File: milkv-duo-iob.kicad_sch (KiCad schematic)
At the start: 18 parts, among them J1 Conn_01x20_Socket, J10 Conn_01x02, J2 Conn_01x20_Socket, J3 Conn_01x05_Socket, J4 8P8C_Shielded, J5 Conn_01x20, J6 Conn_01x20, J7 Conn_01x12, J8 Conn_01x12, J9 Conn_01x04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

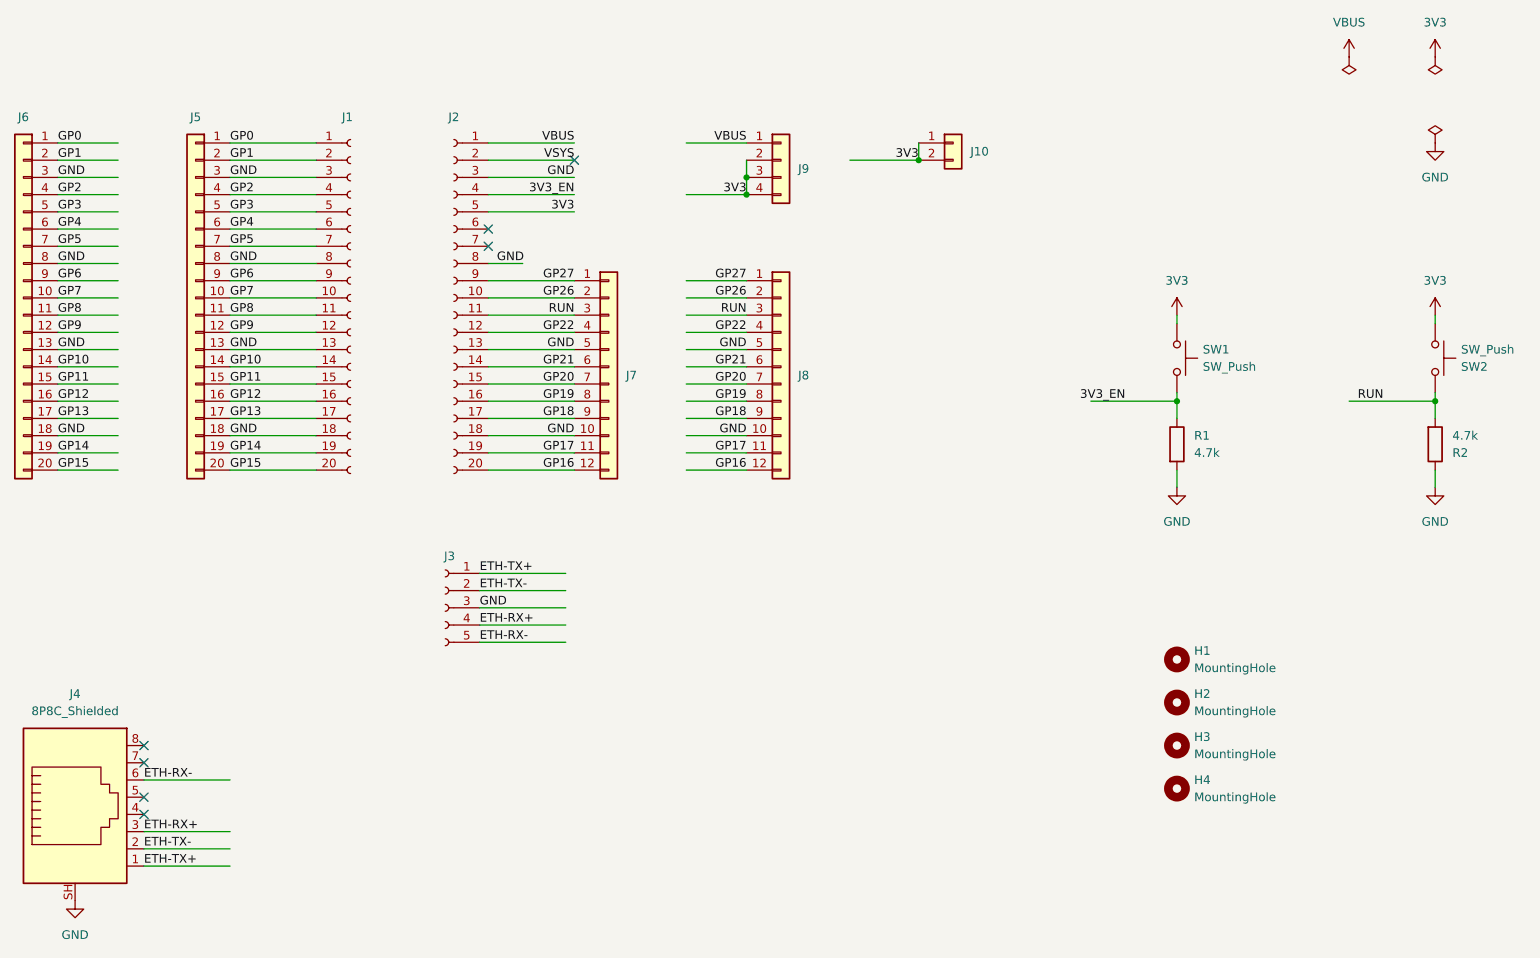
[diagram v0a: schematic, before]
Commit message: Rev.A (今度こそ)
Milk-V Duo の横幅間違えてるし、公式配布の CAD 見ると Ethernet のピンが若干ずれているのも判明
Symbox/footprint 作って対応
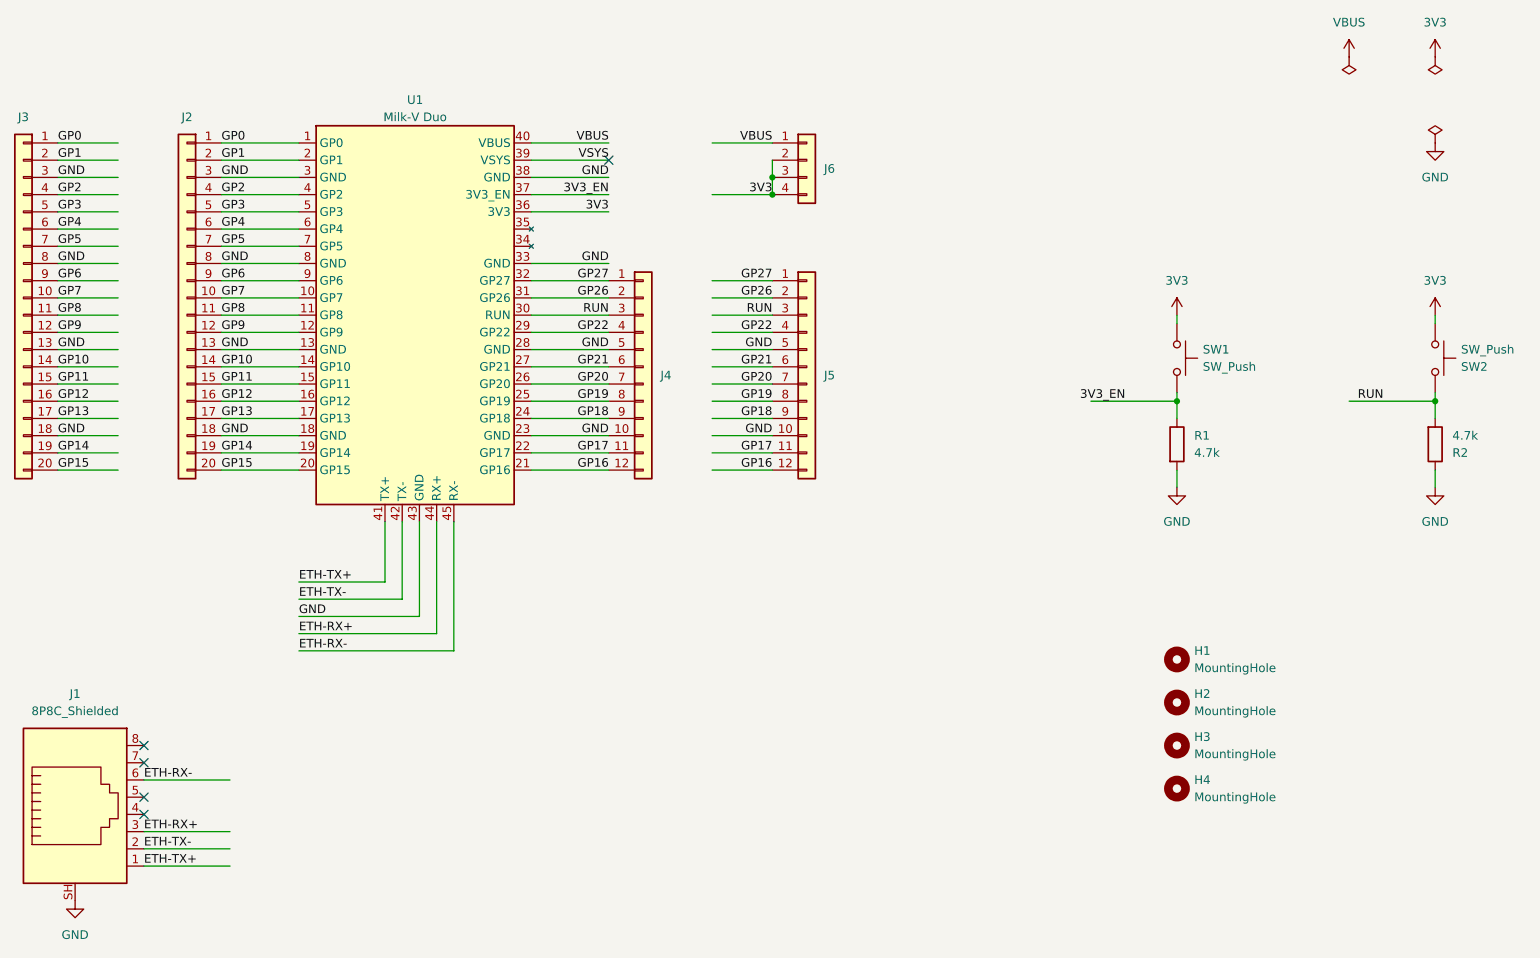
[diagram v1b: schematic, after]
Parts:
- removed J1, J2: Conn_01x20_Socket, Connector_PinSocket_2.54mm:PinSocket_1x20_P2.54mm_Vertical, symbol Connector:Conn_01x20_Socket
- removed J10: Conn_01x02, Connector_PinHeader_2.54mm:PinHeader_1x02_P2.54mm_Vertical, symbol Connector_Generic:Conn_01x02
- removed J3: Conn_01x05_Socket, Connector_PinSocket_2.54mm:PinSocket_1x05_P2.54mm_Vertical, symbol Connector:Conn_01x05_Socket
- added U1: Milk-V Duo, Library:Milk-V_Duo_THT, symbol Library:Milk-V_Duo
- renumbered J4 to J1, J5 to J2, J6 to J3, J7 to J4, J8 to J5, J9 to J6
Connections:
- net 3V3: now also U1.36 (3V3)
- net 3V3_EN: now also U1.37 (3V3_EN)
- net ETH-RX+: now also U1.44 (RX+)
- net ETH-RX-: now also U1.45 (RX-)
- net ETH-TX+: now also U1.41 (TX+)
- net ETH-TX-: now also U1.42 (TX-)
- net GND: now also U1.13 (GND), U1.18 (GND), U1.23 (GND), U1.28 (GND), U1.3 (GND), U1.33 (GND), U1.38 (GND), U1.43 (GND), U1.8 (GND)
- net GP0: now also U1.1 (GP0)
- net GP1: now also U1.2 (GP1)
- net GP10: now also U1.14 (GP10)
- net GP11: now also U1.15 (GP11)
- net GP12: now also U1.16 (GP12)
- net GP13: now also U1.17 (GP13)
- net GP14: now also U1.19 (GP14)
- net GP15: now also U1.20 (GP15)
- net GP16: now also U1.21 (GP16)
- net GP17: now also U1.22 (GP17)
- net GP18: now also U1.24 (GP18)
- net GP19: now also U1.25 (GP19)
- net GP2: now also U1.4 (GP2)
- net GP20: now also U1.26 (GP20)
- net GP21: now also U1.27 (GP21)
- net GP22: now also U1.29 (GP22)
- net GP26: now also U1.31 (GP26)
- net GP27: now also U1.32 (GP27)
- net GP3: now also U1.5 (GP3)
- net GP4: now also U1.6 (GP4)
- net GP5: now also U1.7 (GP5)
- net GP6: now also U1.9 (GP6)
- net GP7: now also U1.10 (GP7)
- net GP8: now also U1.11 (GP8)
- net GP9: now also U1.12 (GP9)
- net RUN: now also U1.30 (RUN)
- net VBUS: now also U1.40 (VBUS)
- net VSYS: now also U1.39 (VSYS)
- no-connect marks 7 -> 5
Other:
- moved on the sheet: J2, J4, J5, J6
